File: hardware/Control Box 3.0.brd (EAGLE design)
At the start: 99.1 x 69.8 mm, 27 parts, among them IC1 LM358N, J1 AC_IN, J2 To_Relay, J3 From_Relay, J4 AC_OUT, J5 To_Reg, J6 From_Reg, J7 54601-908WPLFW/MODEL, K1 T9AS1D22-54PIN, K2 T9AS1D22-54PIN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

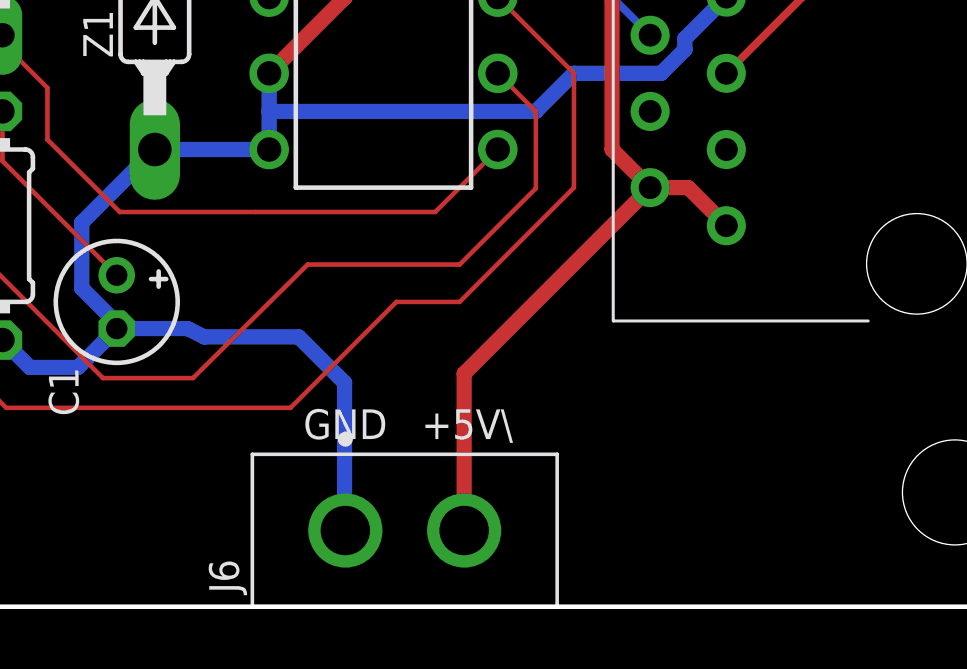
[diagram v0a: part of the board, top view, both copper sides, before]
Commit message: add power indication led to relay module
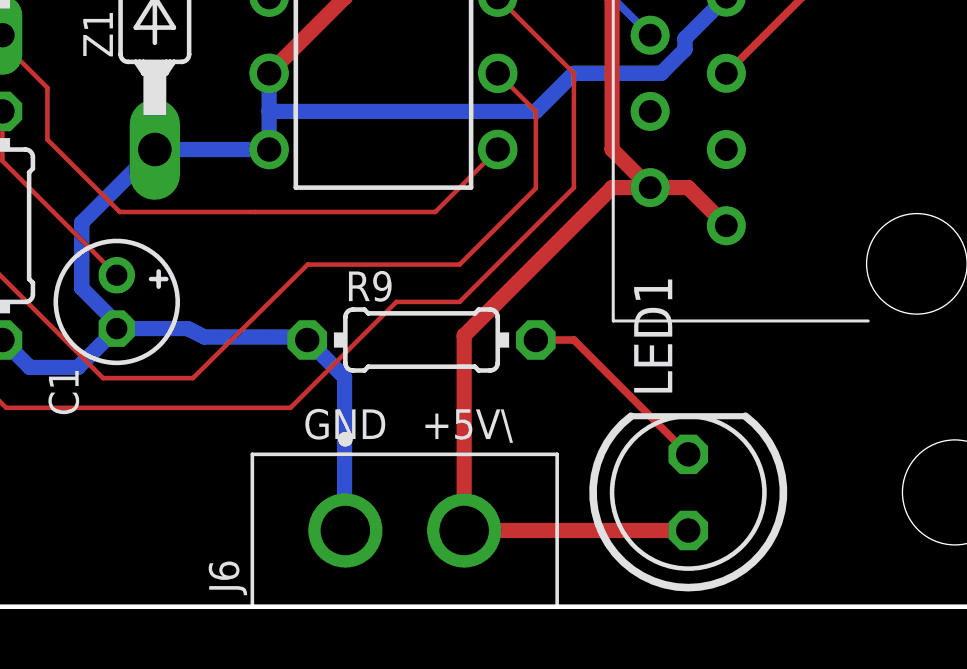
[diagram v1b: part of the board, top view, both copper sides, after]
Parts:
- added LED1: (no value), led:LED5MM
- added R9: 330, mcp:0204/7
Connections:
- new net N$17: LED1.K, R9.2
- net +5V: now also LED1.A
- net GND: now also R9.1
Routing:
- net +5V: track 95.6 -> 103.8 mm
- net N$17: track 0.00 -> 6.66 mm
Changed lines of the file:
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@@
 <attribute name="VALUE" x="76.2" y="19.05" size="0.9906" layer="27" ratio="10" rot="R270" align="center"/>
+</element>
+<element name="LED1" library="led" library_urn="urn:adsk.eagle:library:259" package="LED5MM" package3d_urn="urn:adsk.eagle:package:15799/2" value="" x="86.36" y="3.81" smashed="yes" rot="R90">
+<attribute name="NAME" x="85.8266" y="6.985" size="1.27" layer="25" ratio="10" rot="R90"/>
+<attribute name="VALUE" x="88.1634" y="7.0104" size="1.27" layer="27" ratio="10" rot="R90"/>
+</element>
+<element name="R9" library="mcp" library_urn="urn:adsk.eagle:library:9418757" package="0204/7" package3d_urn="urn:adsk.eagle:package:23498/2" value="330" x="77.47" y="8.89" smashed="yes">
+<attribute name="NAME" x="74.93" y="10.1854" size="0.9906" layer="25" ratio="10"/>
+<attribute name="VALUE" x="75.8444" y="8.4074" size="0.9906" layer="27" ratio="10"/>
 </element>
 </elements>
@@
 <wire x1="68.58" y1="15.24" x2="66.1416" y2="12.8016" width="0.508" layer="16"/>
 <wire x1="67.2846" y1="9.3218" x2="67.31" y2="9.271" width="0.508" layer="16"/>
-<wire x1="74.9046" y1="7.4676" x2="74.9046" y2="2.5908" width="0.508" layer="16"/>
-<wire x1="73.3806" y1="8.9916" x2="74.9046" y2="7.4676" width="0.508" layer="16"/>
-<wire x1="70.231" y1="8.9916" x2="73.3806" y2="8.9916" width="0.508" layer="16"/>
 <wire x1="74.9046" y1="2.5908" x2="74.93" y2="2.54" width="0.508" layer="16"/>
-<wire x1="70.231" y1="8.9916" x2="69.6722" y2="9.271" width="0.508" layer="16"/>
+<wire x1="69.6722" y1="9.271" x2="70.231" y2="8.9916" width="0.508" layer="16"/>
 <wire x1="67.31" y1="9.271" x2="69.6722" y2="9.271" width="0.508" layer="16"/>
 <wire x1="57.4548" y1="8.9916" x2="56.0832" y2="8.9916" width="0.508" layer="16"/>
@@
 <wire x1="74.93" y1="20.32" x2="74.93" y2="23.0632" width="0.508" layer="1"/>
 <wire x1="74.93" y1="23.0632" x2="69.85" y2="28.1432" width="0.508" layer="1"/>
+<contactref element="R9" pad="1"/>
+<wire x1="73.5584" y1="8.9916" x2="73.66" y2="8.89" width="0.508" layer="16"/>
+<wire x1="70.231" y1="8.9916" x2="73.5584" y2="8.9916" width="0.508" layer="16"/>
+<wire x1="73.66" y1="8.89" x2="74.9046" y2="7.6454" width="0.508" layer="16"/>
+<wire x1="74.9046" y1="7.6454" x2="74.9046" y2="2.5908" width="0.508" layer="16"/>
 </signal>
 <signal name="N$3">
@@
 <wire x1="80.01" y1="22.86" x2="75.7682" y2="27.1018" width="0.508" layer="1"/>
 <wire x1="75.7682" y1="27.1018" x2="75.7682" y2="35.56" width="0.508" layer="1"/>
-<wire x1="78.89" y1="2.54" x2="78.89" y2="7.77" width="0.508" layer="1"/>
-<wire x1="78.89" y1="7.77" x2="85.09" y2="13.97" width="0.508" layer="1"/>
+<wire x1="78.89" y1="2.54" x2="78.89" y2="9.04" width="0.508" layer="1"/>
+<wire x1="83.82" y1="13.97" x2="85.09" y2="13.97" width="0.508" layer="1"/>
+<wire x1="83.82" y1="13.97" x2="78.89" y2="9.04" width="0.508" layer="1"/>
+<contactref element="LED1" pad="A"/>
+<wire x1="86.36" y1="2.54" x2="78.89" y2="2.54" width="0.508" layer="1"/>
 </signal>
 <signal name="RELAY_IN">
@@
 <contactref element="K2" pad="3"/>
 </signal>
+<signal name="N$17">
+<contactref element="LED1" pad="K"/>
+<contactref element="R9" pad="2"/>
+<wire x1="81.28" y1="8.89" x2="82.55" y2="8.89" width="0.254" layer="1"/>
+<wire x1="82.55" y1="8.89" x2="86.36" y2="5.08" width="0.254" layer="1"/>
+</signal>
 </signals>

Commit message: fix VH connectors on relay module
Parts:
- moved R9 5.04 mm to (81.3, 5.59), turned to 270 degrees
- moved J6 2.69 mm to (77.5, 3.43), turned to 180 degrees
- moved J5 1.27 mm to (21.6, 14.2)
- moved LED1 1.27 mm to (87.6, 3.81), turned to 180 degrees
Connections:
- net +5V: now also J6.1; no longer J6.2
- net GND: now also J6.2; no longer J6.1
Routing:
- net GND: track 103.9 -> 113.2 mm
- net +5V: track 103.8 -> 105.5 mm
- net N$17: track 6.66 -> 5.92 mm
